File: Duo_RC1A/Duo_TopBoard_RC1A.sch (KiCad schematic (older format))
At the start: 29 parts, among them P1 PIN_ARRAY_2X10, P2 KK3.96_2, Q1 MMBT3904, Q2 MMBT3904

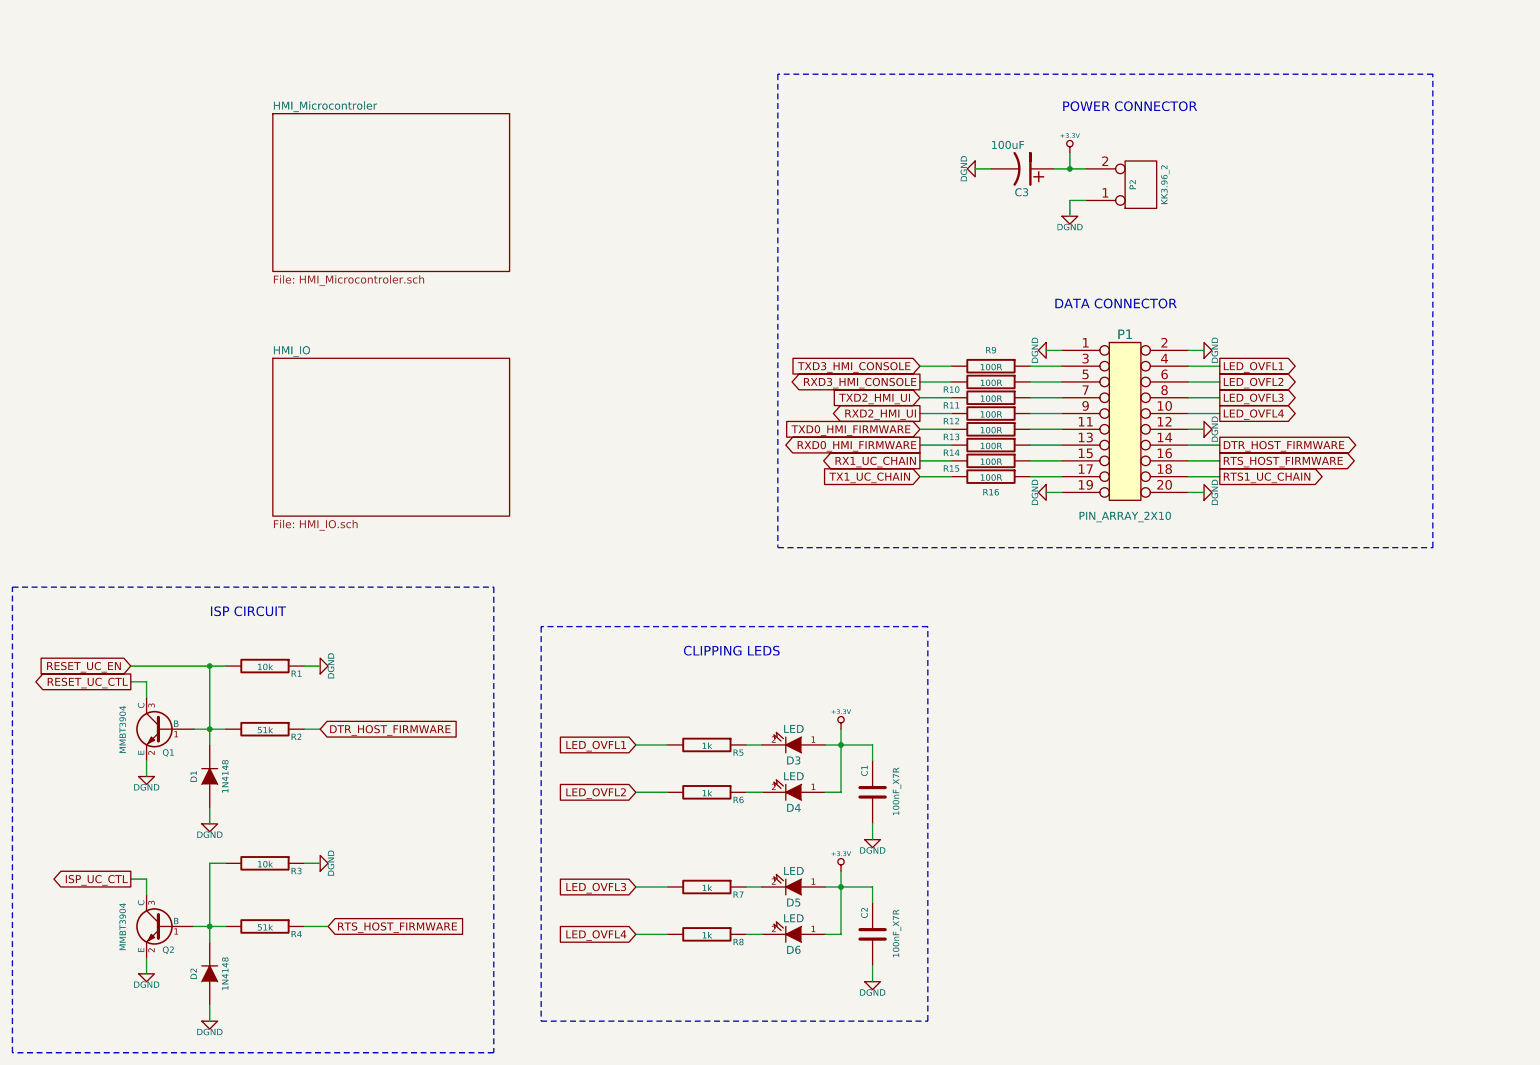
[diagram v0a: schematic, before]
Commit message: PCB dimensions and group placement of all footprints on both BottomBoard and TopBoard layouts.
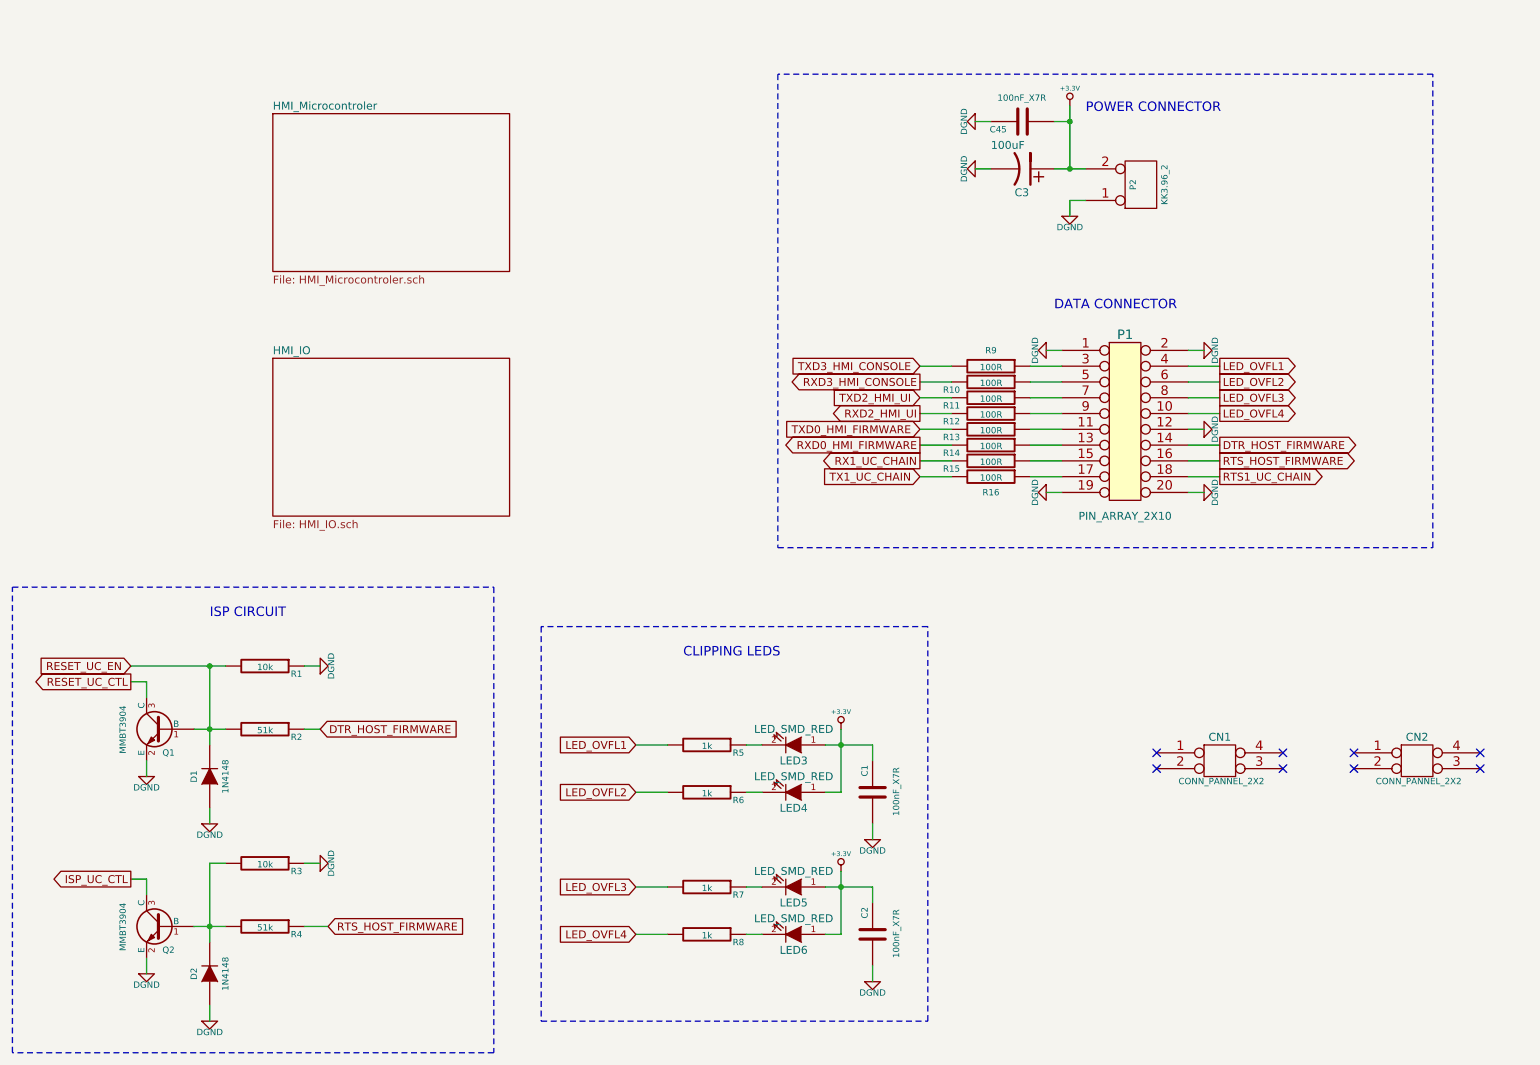
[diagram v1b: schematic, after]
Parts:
- removed D4, D5, D6: LED, Duo_Audio_HMI_RC1A:SM0805, symbol LED
- added C45: 100nF_X7R, Duo_Audio_HMI_RC1A:SM0603, symbol C
- added CN1, CN2: CONN_PANNEL_2X2, Duo_Audio_HMI_RC1A:CONN_PANNEL, symbol CONN_PANNEL_2X2
- added LED4, LED5, LED6: LED_SMD_RED, Duo_Audio_HMI_RC1A:SM0805, symbol LED
- LED3: renamed from D3; value LED -> LED_SMD_RED
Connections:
- net +3.3V: now also C45.2, LED4.1 (A), LED5.1 (A), LED6.1 (A)
- net DGND: now also C45.1
- net at R6.1: now also LED4.2 (K)
- net at R7.1: now also LED5.2 (K)
- net at R8.1: now also LED6.2 (K)
- no-connect marks 0 -> 8
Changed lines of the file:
@@
 L +3.3V #PWR01
 U 1 1 537BD6B8
-P 7500 1800
-F 0 "#PWR01" H 7500 1760 30  0001 C CNN
-F 1 "+3.3V" H 7500 1910 30  0000 C CNN
-F 2 "" H 7500 1800 60  0000 C CNN
-F 3 "" H 7500 1800 60  0000 C CNN
-	1    7500 1800
-	1    0    0    -1
-$EndComp
-Wire Wire Line
-	7500 1800 7500 1900
+P 7500 1500
+F 0 "#PWR01" H 7500 1460 30  0001 C CNN
+F 1 "+3.3V" H 7500 1610 30  0000 C CNN
+F 2 "" H 7500 1500 60  0000 C CNN
+F 3 "" H 7500 1500 60  0000 C CNN
+	1    7500 1500
+	1    0    0    -1
+$EndComp
+Wire Wire Line
+	7500 1500 7500 1900
 Wire Wire Line
 	7400 1900 7600 1900
@@
 $EndComp
 $Comp
-L LED D3
+L LED LED3
 U 1 1 537BE01E
 P 5750 5550
-F 0 "D3" H 5750 5650 50  0000 C CNN
-F 1 "LED" H 5750 5450 50  0000 C CNN
+F 0 "LED3" H 5750 5650 50  0000 C CNN
+F 1 "LED_SMD_RED" H 5750 5450 50  0000 C CNN
 F 2 "Duo_Audio_HMI_RC1A:SM0805" H 5750 5550 60  0001 C CNN
 F 3 "" H 5750 5550 60  0000 C CNN
@@
 	5450 5550 5550 5550
 $Comp
-L LED D4
-U 1 1 537BE097
-P 5750 5850
-F 0 "D4" H 5750 5950 50  0000 C CNN
-F 1 "LED" H 5750 5750 50  0000 C CNN
-F 2 "Duo_Audio_HMI_RC1A:SM0805" H 5750 5850 60  0001 C CNN
-F 3 "" H 5750 5850 60  0000 C CNN
-	1    5750 5850
-	-1   0    0    1
-$EndComp
-$Comp
 L R R6
 U 1 1 537BE09D
@@
 	5450 5850 5550 5850
 $Comp
-L LED D5
-U 1 1 537BE0A4
-P 5750 6450
-F 0 "D5" H 5750 6550 50  0000 C CNN
-F 1 "LED" H 5750 6350 50  0000 C CNN
-F 2 "Duo_Audio_HMI_RC1A:SM0805" H 5750 6450 60  0001 C CNN
-F 3 "" H 5750 6450 60  0000 C CNN
-	1    5750 6450
-	-1   0    0    1
-$EndComp
-$Comp
 L R R7
 U 1 1 537BE0AA
@@
 Wire Wire Line
 	5450 6450 5550 6450
-$Comp
-L LED D6
-U 1 1 537BE0B1
-P 5750 6750
-F 0 "D6" H 5750 6850 50  0000 C CNN
-F 1 "LED" H 5750 6650 50  0000 C CNN
-F 2 "Duo_Audio_HMI_RC1A:SM0805" H 5750 6750 60  0001 C CNN
-F 3 "" H 5750 6750 60  0000 C CNN
-	1    5750 6750
-	-1   0    0    1
-$EndComp
 $Comp
 L R R8
@@
 Text Notes 7400 2800 0    60   ~ 0
 DATA CONNECTOR
-Text Notes 7450 1550 0    60   ~ 0
+Text Notes 7600 1550 0    60   ~ 0
 POWER CONNECTOR
 Text Notes 2050 4750 0    60   ~ 0
@@
 Wire Notes Line
 	9800 1300 5650 1300
+NoConn ~ 8050 5600
+NoConn ~ 8050 5700
+NoConn ~ 8850 5600
+NoConn ~ 8850 5700
+NoConn ~ 9300 5600
+NoConn ~ 9300 5700
+NoConn ~ 10100 5600
+NoConn ~ 10100 5700
+$Comp
+L LED LED4
+U 1 1 5383450B
+P 5750 5850
+F 0 "LED4" H 5750 5950 50  0000 C CNN
+F 1 "LED_SMD_RED" H 5750 5750 50  0000 C CNN
+F 2 "Duo_Audio_HMI_RC1A:SM0805" H 5750 5850 60  0001 C CNN
+F 3 "" H 5750 5850 60  0000 C CNN
+	1    5750 5850
+	-1   0    0    1
+$EndComp
+$Comp
+L LED LED5
+U 1 1 53834516
+P 5750 6450
+F 0 "LED5" H 5750 6550 50  0000 C CNN
+F 1 "LED_SMD_RED" H 5750 6350 50  0000 C CNN
+F 2 "Duo_Audio_HMI_RC1A:SM0805" H 5750 6450 60  0001 C CNN
+F 3 "" H 5750 6450 60  0000 C CNN
+	1    5750 6450
+	-1   0    0    1
+$EndComp
+$Comp
+L LED LED6
+U 1 1 53834521
+P 5750 6750
+F 0 "LED6" H 5750 6850 50  0000 C CNN
+F 1 "LED_SMD_RED" H 5750 6650 50  0000 C CNN
+F 2 "Duo_Audio_HMI_RC1A:SM0805" H 5750 6750 60  0001 C CNN
+F 3 "" H 5750 6750 60  0000 C CNN
+	1    5750 6750
+	-1   0    0    1
+$EndComp
+$Comp
+L CONN_PANNEL_2X2 CN1
+U 1 1 53833E4C
+P 8450 5650
+F 0 "CN1" H 8450 5800 50  0000 C CNN
+F 1 "CONN_PANNEL_2X2" H 8460 5520 40  0000 C CNN
+F 2 "Duo_Audio_HMI_RC1A:CONN_PANNEL" H 8450 5650 60  0001 C CNN
+F 3 "" H 8450 5650 60  0000 C CNN
+	1    8450 5650
+	1    0    0    -1
+$EndComp
+$Comp
+L CONN_PANNEL_2X2 CN2
+U 1 1 53833E72
+P 9700 5650
+F 0 "CN2" H 9700 5800 50  0000 C CNN
+F 1 "CONN_PANNEL_2X2" H 9710 5520 40  0000 C CNN
+F 2 "Duo_Audio_HMI_RC1A:CONN_PANNEL" H 9700 5650 60  0001 C CNN
+F 3 "" H 9700 5650 60  0000 C CNN
+	1    9700 5650
+	1    0    0    -1
+$EndComp
+$Comp
+L C C45
+U 1 1 538344CA
+P 7200 1600
+F 0 "C45" V 7150 1700 40  0000 L CNN
+F 1 "100nF_X7R" V 7350 1450 40  0000 L CNN
+F 2 "Duo_Audio_HMI_RC1A:SM0603" H 7238 1450 30  0001 C CNN
+F 3 "" H 7200 1600 60  0000 C CNN
+	1    7200 1600
+	0    -1   -1   0
+$EndComp
+Wire Wire Line
+	7400 1600 7500 1600
+Connection ~ 7500 1600
+$Comp
+L DGND #PWR019
+U 1 1 53834546
+P 6900 1600
+F 0 "#PWR019" H 6900 1600 40  0001 C CNN
+F 1 "DGND" H 6900 1530 40  0000 C CNN
+F 2 "" H 6900 1600 60  0000 C CNN
+F 3 "" H 6900 1600 60  0000 C CNN
+	1    6900 1600
+	0    1    1    0
+$EndComp
+Wire Wire Line
+	6900 1600 7000 1600
 $EndSCHEMATC

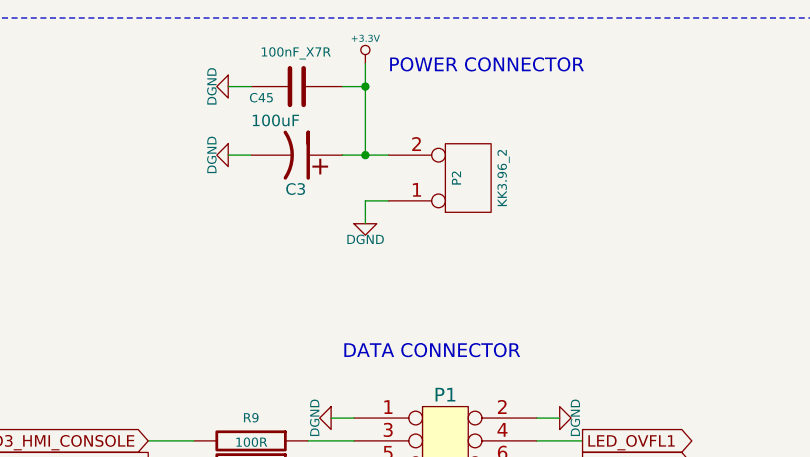
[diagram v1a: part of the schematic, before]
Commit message: Working on the BottomBoard layout. Moved the ITEAD Coreboard to the board left side so there is more space for the linear regulators. Stopped on the USB OTG and USB Host layout.
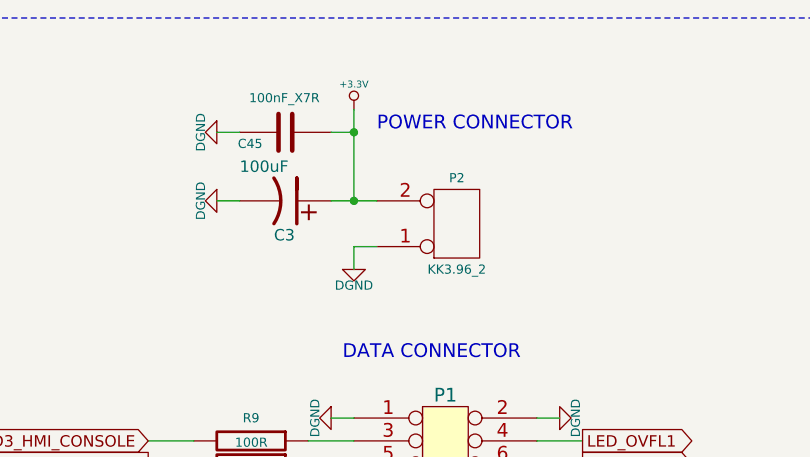
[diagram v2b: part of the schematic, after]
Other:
- moved on the sheet: C3, C45, P2
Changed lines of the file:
@@
 L CONN_2 P2
 U 1 1 537BD1ED
-P 7950 2000
-F 0 "P2" V 7900 2000 40  0000 C CNN
-F 1 "KK3.96_2" V 8100 2000 40  0000 C CNN
-F 2 "Duo_Audio_HMI_RC1A:KK3.96_2PIN" H 7950 2000 60  0001 C CNN
-F 3 "" H 7950 2000 60  0000 C CNN
-	1    7950 2000
+P 7900 2200
+F 0 "P2" H 7900 2000 40  0000 C CNN
+F 1 "KK3.96_2" H 7900 2400 40  0000 C CNN
+F 2 "Duo_Audio_HMI_RC1A:KK3.96_2PIN" H 7900 2200 60  0001 C CNN
+F 3 "" H 7900 2200 60  0000 C CNN
+	1    7900 2200
 	1    0    0    1
 $EndComp
@@
 L +3.3V #PWR01
 U 1 1 537BD6B8
-P 7500 1500
-F 0 "#PWR01" H 7500 1460 30  0001 C CNN
-F 1 "+3.3V" H 7500 1610 30  0000 C CNN
-F 2 "" H 7500 1500 60  0000 C CNN
-F 3 "" H 7500 1500 60  0000 C CNN
-	1    7500 1500
-	1    0    0    -1
-$EndComp
-Wire Wire Line
-	7500 1500 7500 1900
-Wire Wire Line
-	7400 1900 7600 1900
-Wire Wire Line
-	7600 2100 7500 2100
-Wire Wire Line
-	7500 2100 7500 2200
+P 7450 1700
+F 0 "#PWR01" H 7450 1660 30  0001 C CNN
+F 1 "+3.3V" H 7450 1810 30  0000 C CNN
+F 2 "" H 7450 1700 60  0000 C CNN
+F 3 "" H 7450 1700 60  0000 C CNN
+	1    7450 1700
+	1    0    0    -1
+$EndComp
+Wire Wire Line
+	7450 1700 7450 2100
+Wire Wire Line
+	7350 2100 7550 2100
+Wire Wire Line
+	7550 2300 7450 2300
+Wire Wire Line
+	7450 2300 7450 2400
 $Comp
 L DGND #PWR02
 U 1 1 537BD6EB
-P 7500 2200
-F 0 "#PWR02" H 7500 2200 40  0001 C CNN
-F 1 "DGND" H 7500 2130 40  0000 C CNN
-F 2 "" H 7500 2200 60  0000 C CNN
-F 3 "" H 7500 2200 60  0000 C CNN
-	1    7500 2200
+P 7450 2400
+F 0 "#PWR02" H 7450 2400 40  0001 C CNN
+F 1 "DGND" H 7450 2330 40  0000 C CNN
+F 2 "" H 7450 2400 60  0000 C CNN
+F 3 "" H 7450 2400 60  0000 C CNN
+	1    7450 2400
 	1    0    0    -1
 $EndComp
@@
 L CP1 C3
 U 1 1 537BE552
-P 7200 1900
-F 0 "C3" V 7050 1850 50  0000 L CNN
-F 1 "100uF" V 7350 1700 50  0000 L CNN
-F 2 "Duo_Audio_HMI_RC1A:Capacitor5x11RM2" H 7200 1900 60  0001 C CNN
-F 3 "" H 7200 1900 60  0000 C CNN
-	1    7200 1900
+P 7150 2100
+F 0 "C3" V 7000 2050 50  0000 L CNN
+F 1 "100uF" V 7300 1900 50  0000 L CNN
+F 2 "Duo_Audio_HMI_RC1A:Capacitor5x11RM2" H 7150 2100 60  0001 C CNN
+F 3 "" H 7150 2100 60  0000 C CNN
+	1    7150 2100
 	0    1    -1   0
 $EndComp
-Connection ~ 7500 1900
+Connection ~ 7450 2100
 $Comp
 L DGND #PWR08
 U 1 1 537BE5A7
-P 6900 1900
-F 0 "#PWR08" H 6900 1900 40  0001 C CNN
-F 1 "DGND" H 6900 1830 40  0000 C CNN
-F 2 "" H 6900 1900 60  0000 C CNN
-F 3 "" H 6900 1900 60  0000 C CNN
-	1    6900 1900
-	0    1    1    0
-$EndComp
-Wire Wire Line
-	6900 1900 7000 1900
+P 6850 2100
+F 0 "#PWR08" H 6850 2100 40  0001 C CNN
+F 1 "DGND" H 6850 2030 40  0000 C CNN
+F 2 "" H 6850 2100 60  0000 C CNN
+F 3 "" H 6850 2100 60  0000 C CNN
+	1    6850 2100
+	0    1    1    0
+$EndComp
+Wire Wire Line
+	6850 2100 6950 2100
 $Comp
 L BC850 Q2
@@
 Text Notes 7400 2800 0    60   ~ 0
 DATA CONNECTOR
-Text Notes 7600 1550 0    60   ~ 0
+Text Notes 7550 1800 0    60   ~ 0
 POWER CONNECTOR
 Text Notes 2050 4750 0    60   ~ 0
@@
 L C C45
 U 1 1 538344CA
-P 7200 1600
-F 0 "C45" V 7150 1700 40  0000 L CNN
-F 1 "100nF_X7R" V 7350 1450 40  0000 L CNN
-F 2 "Duo_Audio_HMI_RC1A:SM0603" H 7238 1450 30  0001 C CNN
-F 3 "" H 7200 1600 60  0000 C CNN
-	1    7200 1600
+P 7150 1800
+F 0 "C45" V 7100 1900 40  0000 L CNN
+F 1 "100nF_X7R" V 7300 1650 40  0000 L CNN
+F 2 "Duo_Audio_HMI_RC1A:SM0603" H 7188 1650 30  0001 C CNN
+F 3 "" H 7150 1800 60  0000 C CNN
+	1    7150 1800
 	0    -1   -1   0
 $EndComp
 Wire Wire Line
-	7400 1600 7500 1600
-Connection ~ 7500 1600
+	7350 1800 7450 1800
+Connection ~ 7450 1800
 $Comp
 L DGND #PWR019
 U 1 1 53834546
-P 6900 1600
-F 0 "#PWR019" H 6900 1600 40  0001 C CNN
-F 1 "DGND" H 6900 1530 40  0000 C CNN
-F 2 "" H 6900 1600 60  0000 C CNN
-F 3 "" H 6900 1600 60  0000 C CNN
-	1    6900 1600
-	0    1    1    0
-$EndComp
-Wire Wire Line
-	6900 1600 7000 1600
+P 6850 1800
+F 0 "#PWR019" H 6850 1800 40  0001 C CNN
+F 1 "DGND" H 6850 1730 40  0000 C CNN
+F 2 "" H 6850 1800 60  0000 C CNN
+F 3 "" H 6850 1800 60  0000 C CNN
+	1    6850 1800
+	0    1    1    0
+$EndComp
+Wire Wire Line
+	6850 1800 6950 1800
 $EndSCHEMATC
